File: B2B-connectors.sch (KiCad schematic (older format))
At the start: 3 parts, among them J3 DF40C-100DP-0.4V(51), J4 DF40C-100DP-0.4V(51)

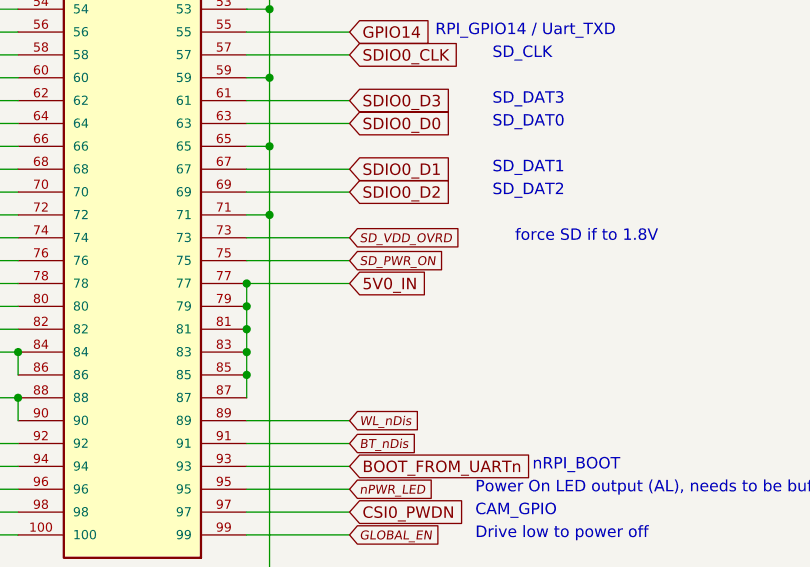
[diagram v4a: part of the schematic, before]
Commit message: Layout - power planes
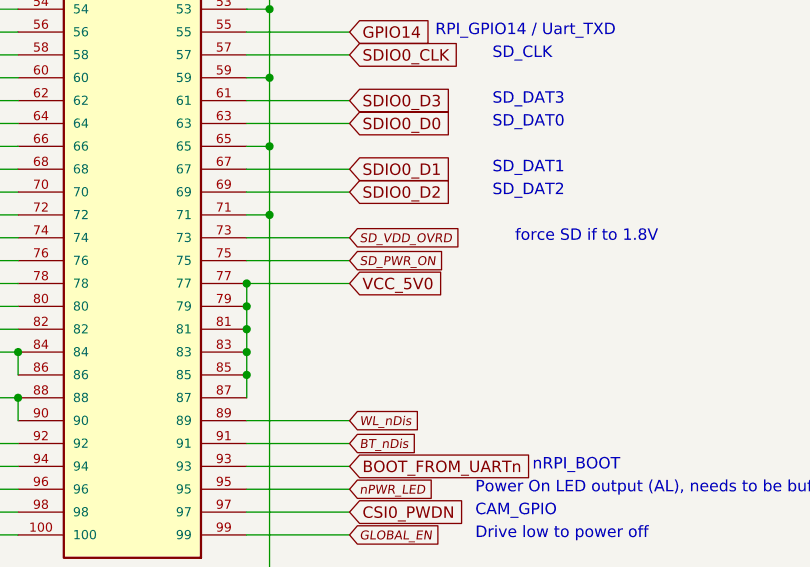
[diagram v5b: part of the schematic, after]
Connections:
- net 5V0_IN renamed VCC_5V0
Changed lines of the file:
@@
 	4800 6200 5250 6200
 Text GLabel 5250 6200 2    50   Input ~ 0
-5V0_IN
+VCC_5V0
 Wire Wire Line
 	4800 7000 5250 7000

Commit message: Replace mounting holes, add revision info to PCB
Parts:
- added MP1, MP2, MP3, MP4: PCB_Mount_Hole_2.5, arvsom-footprints:Mount-hole-M2.5, symbol arvsom:PCB_Mount_Hole_2.5
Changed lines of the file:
@@
 Text GLabel 5250 7000 2    50   Input ~ 0
 BOOT_FROM_UARTn
+$Comp
+L arvsom:PCB_Mount_Hole_2.5 MP1
+U 1 1 60CCB8BB
+P 10650 9800
+F 0 "MP1" H 10858 9846 50  0000 L CNN
+F 1 "PCB_Mount_Hole_2.5" H 10858 9755 50  0000 L CNN
+F 2 "arvsom-footprints:Mount-hole-M2.5" H 11450 10500 50  0001 C CNN
+F 3 "" H 11600 10600 50  0001 C CNN
+	1    10650 9800
+	1    0    0    -1
+$EndComp
+$Comp
+L arvsom:PCB_Mount_Hole_2.5 MP2
+U 1 1 60CCBC95
+P 10650 10175
+F 0 "MP2" H 10858 10221 50  0000 L CNN
+F 1 "PCB_Mount_Hole_2.5" H 10858 10130 50  0000 L CNN
+F 2 "arvsom-footprints:Mount-hole-M2.5" H 11450 10875 50  0001 C CNN
+F 3 "" H 11600 10975 50  0001 C CNN
+	1    10650 10175
+	1    0    0    -1
+$EndComp
+$Comp
+L arvsom:PCB_Mount_Hole_2.5 MP3
+U 1 1 60CCBF28
+P 10650 10550
+F 0 "MP3" H 10858 10596 50  0000 L CNN
+F 1 "PCB_Mount_Hole_2.5" H 10858 10505 50  0000 L CNN
+F 2 "arvsom-footprints:Mount-hole-M2.5" H 11450 11250 50  0001 C CNN
+F 3 "" H 11600 11350 50  0001 C CNN
+	1    10650 10550
+	1    0    0    -1
+$EndComp
+$Comp
+L arvsom:PCB_Mount_Hole_2.5 MP4
+U 1 1 60CCC4ED
+P 10650 10925
+F 0 "MP4" H 10858 10971 50  0000 L CNN
+F 1 "PCB_Mount_Hole_2.5" H 10858 10880 50  0000 L CNN
+F 2 "arvsom-footprints:Mount-hole-M2.5" H 11450 11625 50  0001 C CNN
+F 3 "" H 11600 11725 50  0001 C CNN
+	1    10650 10925
+	1    0    0    -1
+$EndComp
 $EndSCHEMATC
